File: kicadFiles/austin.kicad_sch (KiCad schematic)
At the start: 558 parts, among them J1 Conn_01x04, J2 ARM SWD, J3 TYPE-C-31-M12, Q1 DTC123J, Q2 AO3401A, Q3 DTC123JKAT146, SW1 SW_Push, SW10 MXSwitch, SW100 MXSwitch, SW101 MXSwitch, SW102 MXSwitch, SW103 MXSwitch, SW104 MXSwitch, SW105 MXSwitch, SW106 MXSwitch, SW107 MXSwitch, SW108 MXSwitch, SW109 MXSwitch, SW11 MXSwitch, SW110 MXSwitch, SW111 MXSwitch, SW112 MXSwitch, SW113 MXSwitch, SW114 MXSwitch, SW115 MXSwitch, SW116 MXSwitch, SW12 MXSwitch, SW13 MXSwitch, SW14 MXSwitch, SW15 MXSwitch, SW16 MXSwitch, SW17 MXSwitch, SW18 MXSwitch, SW19 MXSwitch, SW2 PCM12SMTR, SW20 MXSwitch, SW21 MXSwitch, SW22 MXSwitch, SW23 MXSwitch, SW24 MXSwitch, SW25 MXSwitch, SW26 MXSwitch, SW27 MXSwitch, SW28 MXSwitch, SW29 MXSwitch, SW3 MXSwitch, SW30 MXSwitch, SW31 MXSwitch, SW32 MXSwitch, SW33 MXSwitch, SW34 MXSwitch, SW35 MXSwitch, SW36 MXSwitch, SW37 MXSwitch, SW38 MXSwitch, SW39 MXSwitch, SW4 MXSwitch, SW40 MXSwitch, SW41 MXSwitch, SW42 MXSwitch, SW43 MXSwitch, SW44 MXSwitch, SW45 MXSwitch, SW46 MXSwitch, SW47 MXSwitch, SW48 MXSwitch, SW49 MXSwitch, SW5 MXSwitch, SW50 MXSwitch, SW51 MXSwitch, SW52 MXSwitch, SW53 MXSwitch, SW54 MXSwitch, SW55 MXSwitch, SW56 MXSwitch, SW57 MXSwitch, SW58 MXSwitch, SW59 MXSwitch, SW6 MXSwitch, SW60 MXSwitch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

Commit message: Remove switch symbols from bom
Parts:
- SW10, SW100, SW101, SW102, SW103, SW104, SW105, SW106, SW107, SW108, SW109, SW11, SW110, SW111, SW113, SW114, SW115, SW116, SW12, SW13, SW14, SW15, SW16, SW17, SW18, SW19, SW20, SW21, SW22, SW23, SW24, SW25, SW26, SW27, SW28, SW29, SW3, SW30, SW31, SW32, SW33, SW34, SW35, SW36, SW37, SW38, SW39, SW4, SW40, SW41, SW42, SW43, SW44, SW45, SW46, SW47, SW48, SW49, SW5, SW50, SW51, SW52, SW53, SW54, SW55, SW56, SW57, SW58, SW59, SW6, SW60, SW61, SW62, SW63, SW64, SW65, SW66, SW67, SW68, SW69, SW7, SW70, SW71, SW72, SW73, SW74, SW75, SW76, SW77, SW78, SW79, SW8, SW80, SW81, SW82, SW83, SW84, SW85, SW86, SW87, SW88, SW89, SW90, SW91, SW92, SW93, SW94, SW95, SW96, SW97, SW98, SW99: now left out of the parts list

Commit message: Add keyswitch metadata
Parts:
- LED4, LED5: now left out of the parts list
- SW10: symbol austin-rescue:MXSwitch-acheronSymbols-austin-rescue-austin-rescue -> acheronSymbols:MXSwitch; Keycode (none) -> F7; now in the parts list
- SW100: symbol austin-rescue:MXSwitch-acheronSymbols-austin-rescue-austin-rescue -> acheronSymbols:MXSwitch; Keycode (none) -> NPLUS; now in the parts list
- SW101: symbol austin-rescue:MXSwitch-acheronSymbols-austin-rescue-austin-rescue -> acheronSymbols:MXSwitch; Keycode (none) -> (625) LCTRL; now in the parts list
- SW102: symbol austin-rescue:MXSwitch-acheronSymbols-austin-rescue-austin-rescue -> acheronSymbols:MXSwitch; Keycode (none) -> (625) LWIN; now in the parts list
- SW103: symbol austin-rescue:MXSwitch-acheronSymbols-austin-rescue-austin-rescue -> acheronSymbols:MXSwitch; Keycode (none) -> (625) SPC; now in the parts list
- SW104: symbol austin-rescue:MXSwitch-acheronSymbols-austin-rescue-austin-rescue -> acheronSymbols:MXSwitch; Keycode (none) -> RALT; now in the parts list
- SW105: symbol austin-rescue:MXSwitch-acheronSymbols-austin-rescue-austin-rescue -> acheronSymbols:MXSwitch; Keycode (none) -> RWIN; now in the parts list
- SW106: symbol austin-rescue:MXSwitch-acheronSymbols-austin-rescue-austin-rescue -> acheronSymbols:MXSwitch; Keycode (none) -> LEFT; now in the parts list
- SW107: symbol austin-rescue:MXSwitch-acheronSymbols-austin-rescue-austin-rescue -> acheronSymbols:MXSwitch; Keycode (none) -> DOWN; now in the parts list
- SW108: symbol austin-rescue:MXSwitch-acheronSymbols-austin-rescue-austin-rescue -> acheronSymbols:MXSwitch; Keycode (none) -> LZERO; now in the parts list
- SW109: symbol austin-rescue:MXSwitch-acheronSymbols-austin-rescue-austin-rescue -> acheronSymbols:MXSwitch; Keycode (none) -> RZERO; now in the parts list
- SW11: symbol austin-rescue:MXSwitch-acheronSymbols-austin-rescue-austin-rescue -> acheronSymbols:MXSwitch; Keycode (none) -> F8; now in the parts list
- SW110: symbol austin-rescue:MXSwitch-acheronSymbols-austin-rescue-austin-rescue -> acheronSymbols:MXSwitch; Keycode (none) -> N0; now in the parts list
- SW111: symbol austin-rescue:MXSwitch-acheronSymbols-austin-rescue-austin-rescue -> acheronSymbols:MXSwitch; Keycode (none) -> (700) RCTRL; now in the parts list
- SW112: symbol austin-rescue:MXSwitch-acheronSymbols-austin-rescue-austin-rescue -> acheronSymbols:MXSwitch; Keycode (none) -> (700) LALT
- SW113: symbol austin-rescue:MXSwitch-acheronSymbols-austin-rescue-austin-rescue -> acheronSymbols:MXSwitch; Keycode (none) -> (625) LALT; now in the parts list
- SW114: symbol austin-rescue:MXSwitch-acheronSymbols-austin-rescue-austin-rescue -> acheronSymbols:MXSwitch; Keycode (none) -> (700) SPC; now in the parts list
- SW115: symbol austin-rescue:MXSwitch-acheronSymbols-austin-rescue-austin-rescue -> acheronSymbols:MXSwitch; Keycode (none) -> RIGHT; now in the parts list
- SW116: symbol austin-rescue:MXSwitch-acheronSymbols-austin-rescue-austin-rescue -> acheronSymbols:MXSwitch; Keycode (none) -> 2UZERO; now in the parts list
- SW12: symbol austin-rescue:MXSwitch-acheronSymbols-austin-rescue-austin-rescue -> acheronSymbols:MXSwitch; Keycode (none) -> F9; now in the parts list
- SW13: symbol austin-rescue:MXSwitch-acheronSymbols-austin-rescue-austin-rescue -> acheronSymbols:MXSwitch; Keycode (none) -> F10; now in the parts list
- SW14: symbol austin-rescue:MXSwitch-acheronSymbols-austin-rescue-austin-rescue -> acheronSymbols:MXSwitch; Keycode (none) -> F11; now in the parts list
- SW15: symbol austin-rescue:MXSwitch-acheronSymbols-austin-rescue-austin-rescue -> acheronSymbols:MXSwitch; Keycode (none) -> F12; now in the parts list
- SW16: symbol austin-rescue:MXSwitch-acheronSymbols-austin-rescue-austin-rescue -> acheronSymbols:MXSwitch; Keycode (none) -> F13; now in the parts list
- SW17: symbol austin-rescue:MXSwitch-acheronSymbols-austin-rescue-austin-rescue -> acheronSymbols:MXSwitch; Keycode (none) -> SCRLK; now in the parts list
- SW18: symbol austin-rescue:MXSwitch-acheronSymbols-austin-rescue-austin-rescue -> acheronSymbols:MXSwitch; Keycode (none) -> PAUSE; now in the parts list
- SW19: symbol austin-rescue:MXSwitch-acheronSymbols-austin-rescue-austin-rescue -> acheronSymbols:MXSwitch; Keycode (none) -> HOME; now in the parts list
- SW20: symbol austin-rescue:MXSwitch-acheronSymbols-austin-rescue-austin-rescue -> acheronSymbols:MXSwitch; Keycode (none) -> END; now in the parts list
- SW21: symbol austin-rescue:MXSwitch-acheronSymbols-austin-rescue-austin-rescue -> acheronSymbols:MXSwitch; Keycode (none) -> DELETE; now in the parts list
- SW22: symbol austin-rescue:MXSwitch-acheronSymbols-austin-rescue-austin-rescue -> acheronSymbols:MXSwitch; Keycode (none) -> GRAVE; now in the parts list
- SW23: symbol austin-rescue:MXSwitch-acheronSymbols-austin-rescue-austin-rescue -> acheronSymbols:MXSwitch; Keycode (none) -> 1; now in the parts list
- SW24: symbol austin-rescue:MXSwitch-acheronSymbols-austin-rescue-austin-rescue -> acheronSymbols:MXSwitch; Keycode (none) -> 2; now in the parts list
- SW25: symbol austin-rescue:MXSwitch-acheronSymbols-austin-rescue-austin-rescue -> acheronSymbols:MXSwitch; Keycode (none) -> 3; now in the parts list
- SW26: symbol austin-rescue:MXSwitch-acheronSymbols-austin-rescue-austin-rescue -> acheronSymbols:MXSwitch; Keycode (none) -> 4; now in the parts list
- SW27: symbol austin-rescue:MXSwitch-acheronSymbols-austin-rescue-austin-rescue -> acheronSymbols:MXSwitch; Keycode (none) -> 5; now in the parts list
- SW28: symbol austin-rescue:MXSwitch-acheronSymbols-austin-rescue-austin-rescue -> acheronSymbols:MXSwitch; Keycode (none) -> 6; now in the parts list
- SW29: symbol austin-rescue:MXSwitch-acheronSymbols-austin-rescue-austin-rescue -> acheronSymbols:MXSwitch; Keycode (none) -> 7; now in the parts list
- SW3: symbol austin-rescue:MXSwitch-acheronSymbols-austin-rescue-austin-rescue -> acheronSymbols:MXSwitch; Keycode (none) -> ESC; now in the parts list
- SW30: symbol austin-rescue:MXSwitch-acheronSymbols-austin-rescue-austin-rescue -> acheronSymbols:MXSwitch; Keycode (none) -> 8; now in the parts list
- SW31: symbol austin-rescue:MXSwitch-acheronSymbols-austin-rescue-austin-rescue -> acheronSymbols:MXSwitch; Keycode (none) -> 9; now in the parts list
- SW32: symbol austin-rescue:MXSwitch-acheronSymbols-austin-rescue-austin-rescue -> acheronSymbols:MXSwitch; Keycode (none) -> 0; now in the parts list
- SW33: symbol austin-rescue:MXSwitch-acheronSymbols-austin-rescue-austin-rescue -> acheronSymbols:MXSwitch; Keycode (none) -> MINUS; now in the parts list
- SW34: symbol austin-rescue:MXSwitch-acheronSymbols-austin-rescue-austin-rescue -> acheronSymbols:MXSwitch; Keycode (none) -> EQL; now in the parts list
- SW35: symbol austin-rescue:MXSwitch-acheronSymbols-austin-rescue-austin-rescue -> acheronSymbols:MXSwitch; Keycode (none) -> LBKSP; now in the parts list
- SW36: symbol austin-rescue:MXSwitch-acheronSymbols-austin-rescue-austin-rescue -> acheronSymbols:MXSwitch; Keycode (none) -> RBKSP; now in the parts list
- SW37: symbol austin-rescue:MXSwitch-acheronSymbols-austin-rescue-austin-rescue -> acheronSymbols:MXSwitch; Keycode (none) -> INS; now in the parts list
- SW38: symbol austin-rescue:MXSwitch-acheronSymbols-austin-rescue-austin-rescue -> acheronSymbols:MXSwitch; Keycode (none) -> NUMLK; now in the parts list
- SW39: symbol austin-rescue:MXSwitch-acheronSymbols-austin-rescue-austin-rescue -> acheronSymbols:MXSwitch; Keycode (none) -> NSLS; now in the parts list
- SW4: symbol austin-rescue:MXSwitch-acheronSymbols-austin-rescue-austin-rescue -> acheronSymbols:MXSwitch; Keycode (none) -> F1; now in the parts list
- SW40: symbol austin-rescue:MXSwitch-acheronSymbols-austin-rescue-austin-rescue -> acheronSymbols:MXSwitch; Keycode (none) -> NMUL; now in the parts list
- SW41: symbol austin-rescue:MXSwitch-acheronSymbols-austin-rescue-austin-rescue -> acheronSymbols:MXSwitch; Keycode (none) -> FULLBKSP; now in the parts list
- SW42: symbol austin-rescue:MXSwitch-acheronSymbols-austin-rescue-austin-rescue -> acheronSymbols:MXSwitch; Keycode (none) -> ISOENTER; now in the parts list
- SW43: symbol austin-rescue:MXSwitch-acheronSymbols-austin-rescue-austin-rescue -> acheronSymbols:MXSwitch; Keycode (none) -> TAB; now in the parts list
- SW44: symbol austin-rescue:MXSwitch-acheronSymbols-austin-rescue-austin-rescue -> acheronSymbols:MXSwitch; Keycode (none) -> Q; now in the parts list
- SW45: symbol austin-rescue:MXSwitch-acheronSymbols-austin-rescue-austin-rescue -> acheronSymbols:MXSwitch; Keycode (none) -> W; now in the parts list
- SW46: symbol austin-rescue:MXSwitch-acheronSymbols-austin-rescue-austin-rescue -> acheronSymbols:MXSwitch; Keycode (none) -> E; now in the parts list
- SW47: symbol austin-rescue:MXSwitch-acheronSymbols-austin-rescue-austin-rescue -> acheronSymbols:MXSwitch; Keycode (none) -> R; now in the parts list
- SW48: symbol austin-rescue:MXSwitch-acheronSymbols-austin-rescue-austin-rescue -> acheronSymbols:MXSwitch; Keycode (none) -> T; now in the parts list
- SW49: symbol austin-rescue:MXSwitch-acheronSymbols-austin-rescue-austin-rescue -> acheronSymbols:MXSwitch; Keycode (none) -> Y; now in the parts list
- SW5: symbol austin-rescue:MXSwitch-acheronSymbols-austin-rescue-austin-rescue -> acheronSymbols:MXSwitch; Keycode (none) -> F2; now in the parts list
- SW50: symbol austin-rescue:MXSwitch-acheronSymbols-austin-rescue-austin-rescue -> acheronSymbols:MXSwitch; Keycode (none) -> U; now in the parts list
- SW51: symbol austin-rescue:MXSwitch-acheronSymbols-austin-rescue-austin-rescue -> acheronSymbols:MXSwitch; Keycode (none) -> I; now in the parts list
- SW52: symbol austin-rescue:MXSwitch-acheronSymbols-austin-rescue-austin-rescue -> acheronSymbols:MXSwitch; Keycode (none) -> O; now in the parts list
- SW53: symbol austin-rescue:MXSwitch-acheronSymbols-austin-rescue-austin-rescue -> acheronSymbols:MXSwitch; Keycode (none) -> P; now in the parts list
- SW54: symbol austin-rescue:MXSwitch-acheronSymbols-austin-rescue-austin-rescue -> acheronSymbols:MXSwitch; Keycode (none) -> LBRKT; now in the parts list
- SW55: symbol austin-rescue:MXSwitch-acheronSymbols-austin-rescue-austin-rescue -> acheronSymbols:MXSwitch; Keycode (none) -> RBRKT; now in the parts list
- SW56: symbol austin-rescue:MXSwitch-acheronSymbols-austin-rescue-austin-rescue -> acheronSymbols:MXSwitch; Keycode (none) -> BSLS; now in the parts list
- SW57: symbol austin-rescue:MXSwitch-acheronSymbols-austin-rescue-austin-rescue -> acheronSymbols:MXSwitch; Keycode (none) -> PGUP; now in the parts list
- SW58: symbol austin-rescue:MXSwitch-acheronSymbols-austin-rescue-austin-rescue -> acheronSymbols:MXSwitch; Keycode (none) -> N7; now in the parts list
- SW59: symbol austin-rescue:MXSwitch-acheronSymbols-austin-rescue-austin-rescue -> acheronSymbols:MXSwitch; Keycode (none) -> N8; now in the parts list
- SW6: symbol austin-rescue:MXSwitch-acheronSymbols-austin-rescue-austin-rescue -> acheronSymbols:MXSwitch; Keycode (none) -> F3; now in the parts list
- SW60: symbol austin-rescue:MXSwitch-acheronSymbols-austin-rescue-austin-rescue -> acheronSymbols:MXSwitch; Keycode (none) -> N9; now in the parts list
- SW61: symbol austin-rescue:MXSwitch-acheronSymbols-austin-rescue-austin-rescue -> acheronSymbols:MXSwitch; Keycode (none) -> NMINUS; now in the parts list
- SW62: symbol austin-rescue:MXSwitch-acheronSymbols-austin-rescue-austin-rescue -> acheronSymbols:MXSwitch; Keycode (none) -> ISOTILDE; now in the parts list
- SW63: symbol austin-rescue:MXSwitch-acheronSymbols-austin-rescue-austin-rescue -> acheronSymbols:MXSwitch; Keycode (none) -> CAPS; now in the parts list
- SW64: symbol austin-rescue:MXSwitch-acheronSymbols-austin-rescue-austin-rescue -> acheronSymbols:MXSwitch; Keycode (none) -> A; now in the parts list
- SW65: symbol austin-rescue:MXSwitch-acheronSymbols-austin-rescue-austin-rescue -> acheronSymbols:MXSwitch; Keycode (none) -> S; now in the parts list
- SW66: symbol austin-rescue:MXSwitch-acheronSymbols-austin-rescue-austin-rescue -> acheronSymbols:MXSwitch; Keycode (none) -> D; now in the parts list
- SW67: symbol austin-rescue:MXSwitch-acheronSymbols-austin-rescue-austin-rescue -> acheronSymbols:MXSwitch; Keycode (none) -> F; now in the parts list
- SW68: symbol austin-rescue:MXSwitch-acheronSymbols-austin-rescue-austin-rescue -> acheronSymbols:MXSwitch; Keycode (none) -> G; now in the parts list
- SW69: symbol austin-rescue:MXSwitch-acheronSymbols-austin-rescue-austin-rescue -> acheronSymbols:MXSwitch; Keycode (none) -> H; now in the parts list
- SW7: symbol austin-rescue:MXSwitch-acheronSymbols-austin-rescue-austin-rescue -> acheronSymbols:MXSwitch; Keycode (none) -> F4; now in the parts list
- SW70: symbol austin-rescue:MXSwitch-acheronSymbols-austin-rescue-austin-rescue -> acheronSymbols:MXSwitch; Keycode (none) -> J; now in the parts list
- SW71: symbol austin-rescue:MXSwitch-acheronSymbols-austin-rescue-austin-rescue -> acheronSymbols:MXSwitch; Keycode (none) -> K; now in the parts list
- SW72: symbol austin-rescue:MXSwitch-acheronSymbols-austin-rescue-austin-rescue -> acheronSymbols:MXSwitch; Keycode (none) -> L; now in the parts list
- SW73: symbol austin-rescue:MXSwitch-acheronSymbols-austin-rescue-austin-rescue -> acheronSymbols:MXSwitch; Keycode (none) -> COLON; now in the parts list
- SW74: symbol austin-rescue:MXSwitch-acheronSymbols-austin-rescue-austin-rescue -> acheronSymbols:MXSwitch; Keycode (none) -> QUOTE; now in the parts list
- SW75: symbol austin-rescue:MXSwitch-acheronSymbols-austin-rescue-austin-rescue -> acheronSymbols:MXSwitch; Keycode (none) -> ANSIENTER; now in the parts list
- SW76: symbol austin-rescue:MXSwitch-acheronSymbols-austin-rescue-austin-rescue -> acheronSymbols:MXSwitch; Keycode (none) -> PGDN; now in the parts list
- SW77: symbol austin-rescue:MXSwitch-acheronSymbols-austin-rescue-austin-rescue -> acheronSymbols:MXSwitch; Keycode (none) -> N4; now in the parts list
- SW78: symbol austin-rescue:MXSwitch-acheronSymbols-austin-rescue-austin-rescue -> acheronSymbols:MXSwitch; Keycode (none) -> N5; now in the parts list
- SW79: symbol austin-rescue:MXSwitch-acheronSymbols-austin-rescue-austin-rescue -> acheronSymbols:MXSwitch; Keycode (none) -> N6; now in the parts list
- SW8: symbol austin-rescue:MXSwitch-acheronSymbols-austin-rescue-austin-rescue -> acheronSymbols:MXSwitch; Keycode (none) -> F5; now in the parts list
- SW80: symbol austin-rescue:MXSwitch-acheronSymbols-austin-rescue-austin-rescue -> acheronSymbols:MXSwitch; Keycode (none) -> NENTER; now in the parts list
- SW81: symbol austin-rescue:MXSwitch-acheronSymbols-austin-rescue-austin-rescue -> acheronSymbols:MXSwitch; Keycode (none) -> STEPPEDCAPS; now in the parts list
- SW82: value ANSI LShift -> MXSwitch; symbol austin-rescue:MXSwitch-acheronSymbols-austin-rescue-austin-rescue -> acheronSymbols:MXSwitch; Keycode (none) -> ANSISHIFT; now in the parts list
- SW83: symbol austin-rescue:MXSwitch-acheronSymbols-austin-rescue-austin-rescue -> acheronSymbols:MXSwitch; Keycode (none) -> RSFT; now in the parts list
- SW84: value ISO LShift -> MXSwitch; symbol austin-rescue:MXSwitch-acheronSymbols-austin-rescue-austin-rescue -> acheronSymbols:MXSwitch; Keycode (none) -> ISOSHIFT; now in the parts list
- SW85: value ISO Slash -> MXSwitch; symbol austin-rescue:MXSwitch-acheronSymbols-austin-rescue-austin-rescue -> acheronSymbols:MXSwitch; Keycode (none) -> ISOSLS; now in the parts list
- SW86: symbol austin-rescue:MXSwitch-acheronSymbols-austin-rescue-austin-rescue -> acheronSymbols:MXSwitch; Keycode (none) -> Z; now in the parts list
- SW87: symbol austin-rescue:MXSwitch-acheronSymbols-austin-rescue-austin-rescue -> acheronSymbols:MXSwitch; Keycode (none) -> X; now in the parts list
- SW88: symbol austin-rescue:MXSwitch-acheronSymbols-austin-rescue-austin-rescue -> acheronSymbols:MXSwitch; Keycode (none) -> C; now in the parts list
- SW89: symbol austin-rescue:MXSwitch-acheronSymbols-austin-rescue-austin-rescue -> acheronSymbols:MXSwitch; Keycode (none) -> V; now in the parts list
- SW9: symbol austin-rescue:MXSwitch-acheronSymbols-austin-rescue-austin-rescue -> acheronSymbols:MXSwitch; Keycode (none) -> F6
- SW90: symbol austin-rescue:MXSwitch-acheronSymbols-austin-rescue-austin-rescue -> acheronSymbols:MXSwitch; Keycode (none) -> B; now in the parts list
- SW91: symbol austin-rescue:MXSwitch-acheronSymbols-austin-rescue-austin-rescue -> acheronSymbols:MXSwitch; Keycode (none) -> N; now in the parts list
- SW92: symbol austin-rescue:MXSwitch-acheronSymbols-austin-rescue-austin-rescue -> acheronSymbols:MXSwitch; Keycode (none) -> M; now in the parts list
- SW93: symbol austin-rescue:MXSwitch-acheronSymbols-austin-rescue-austin-rescue -> acheronSymbols:MXSwitch; Keycode (none) -> COMMA; now in the parts list
- SW94: symbol austin-rescue:MXSwitch-acheronSymbols-austin-rescue-austin-rescue -> acheronSymbols:MXSwitch; Keycode (none) -> DOT; now in the parts list
- SW95: symbol austin-rescue:MXSwitch-acheronSymbols-austin-rescue-austin-rescue -> acheronSymbols:MXSwitch; Keycode (none) -> SLS; now in the parts list
- SW96: symbol austin-rescue:MXSwitch-acheronSymbols-austin-rescue-austin-rescue -> acheronSymbols:MXSwitch; Keycode (none) -> UP; now in the parts list
- SW97: symbol austin-rescue:MXSwitch-acheronSymbols-austin-rescue-austin-rescue -> acheronSymbols:MXSwitch; Keycode (none) -> N1; now in the parts list
- SW98: symbol austin-rescue:MXSwitch-acheronSymbols-austin-rescue-austin-rescue -> acheronSymbols:MXSwitch; Keycode (none) -> N2; now in the parts list
- SW99: symbol austin-rescue:MXSwitch-acheronSymbols-austin-rescue-austin-rescue -> acheronSymbols:MXSwitch; Keycode (none) -> N3; now in the parts list
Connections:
- net Col13: now also SW106.1 (Col)
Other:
- note removed: """
- note removed: "*"
- note removed: "+"
- note removed: "+="
- note removed: "-"
- note removed: "-_"
- note removed: "/"
- note removed: "0"
- note removed: "2"
- note removed: "3"
- note removed: "4"
- note removed: "5"
- note removed: "6"
- note removed: "7"
- note removed: "8"
- note removed: "9"
- note removed: ":;"
- note removed: "A"
- note removed: "B1LAlt"
- note removed: "B1RAlt"
- note removed: "B1RCtrl"
- note removed: "B1Spc"
- note removed: "B2LCtrl"
- note removed: "B2LWin"
- note removed: "B2Spc"
- note removed: "Backspace"
- note removed: "Caps"
- note removed: "D"
- note removed: "Del"
- note removed: "Delete"
- note removed: "Down"
- note removed: "End"
- note removed: "Enter"
- note removed: "Esc"
- note removed: "F1"
- note removed: "F10"
- note removed: "F11"
- note removed: "F12"
- note removed: "F2"
- note removed: "F3"
- note removed: "F4"
- note removed: "F5"
- note removed: "F6"
- note removed: "F7"
- note removed: "F8"
- note removed: "F9"
- note removed: "G"
- note removed: "GRAVE"
- note removed: "H"
- note removed: "Home"
- note removed: "ISO Enter"
- note removed: "ISO Tilde"
- note removed: "Insert"
- note removed: "J"
- note removed: "K"
- note removed: "L"
- note removed: "Left"
- note removed: "Numlock"
- note removed: "Pause"
- note removed: "PgDwn"
- note removed: "PgUp"
- note removed: "PrtSc"
- note removed: "R1Alt"
- note removed: "R1Win"
- note removed: "Right"
- note removed: "S"
- note removed: "ScrLck"
- note removed: "Split0L"
- note removed: "Split0R"
- note removed: "SplitBsL"
- note removed: "SplitBsR"
- note removed: "Stepped Caps"
- note removed: "\|"

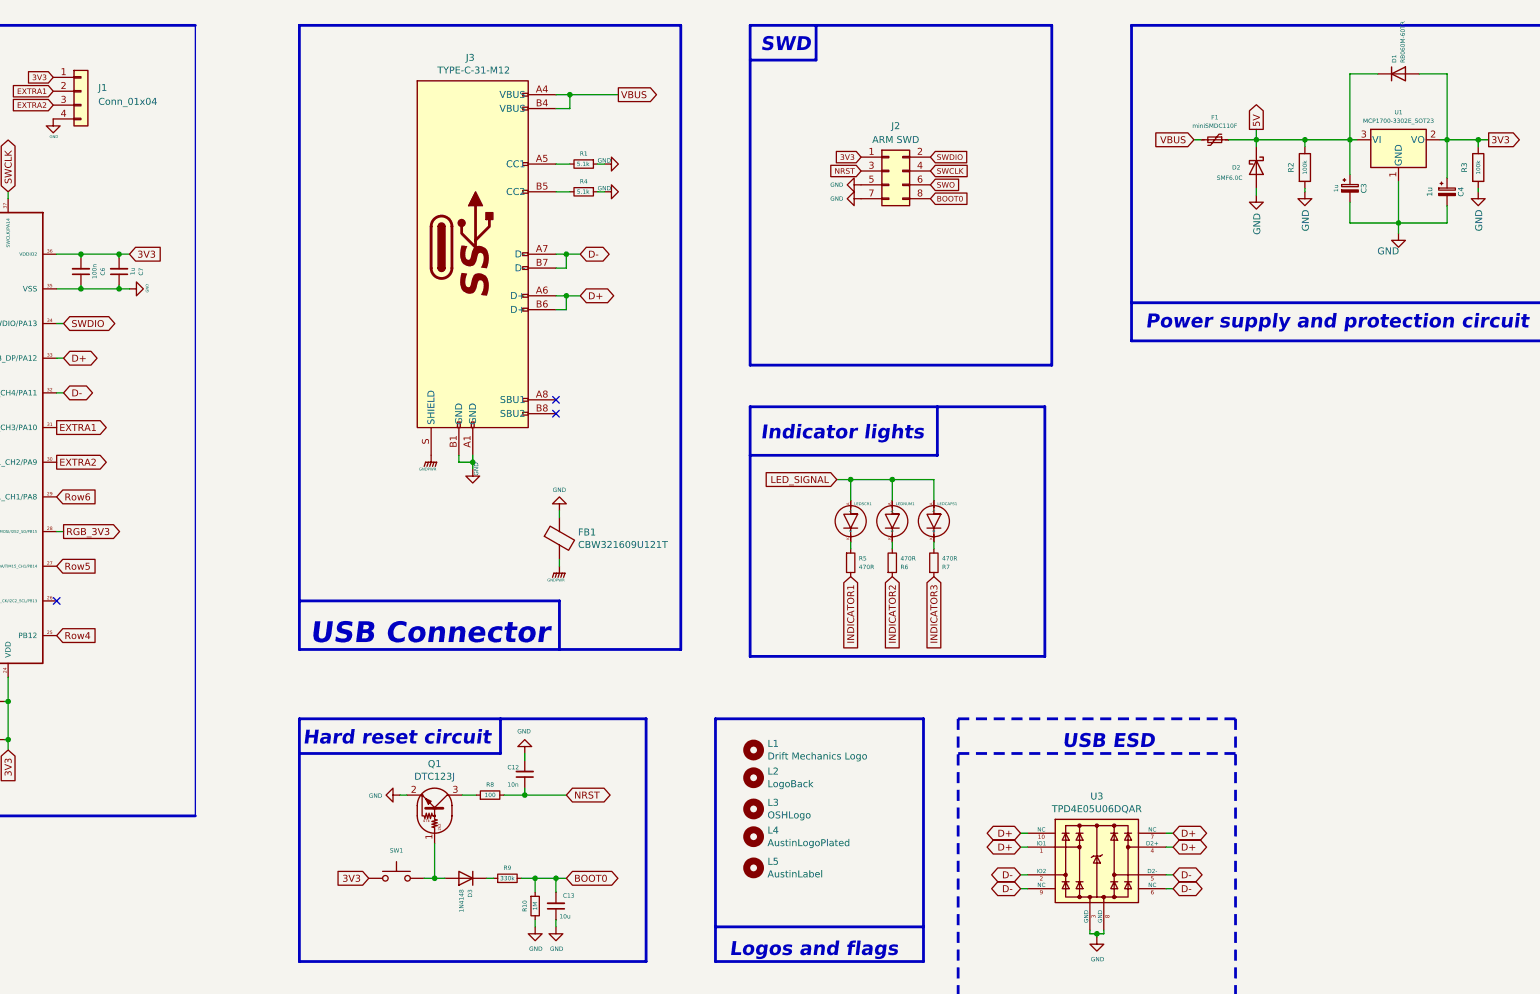
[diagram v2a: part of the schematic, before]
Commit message: Add component metadata, remove THT LEDs from BOM
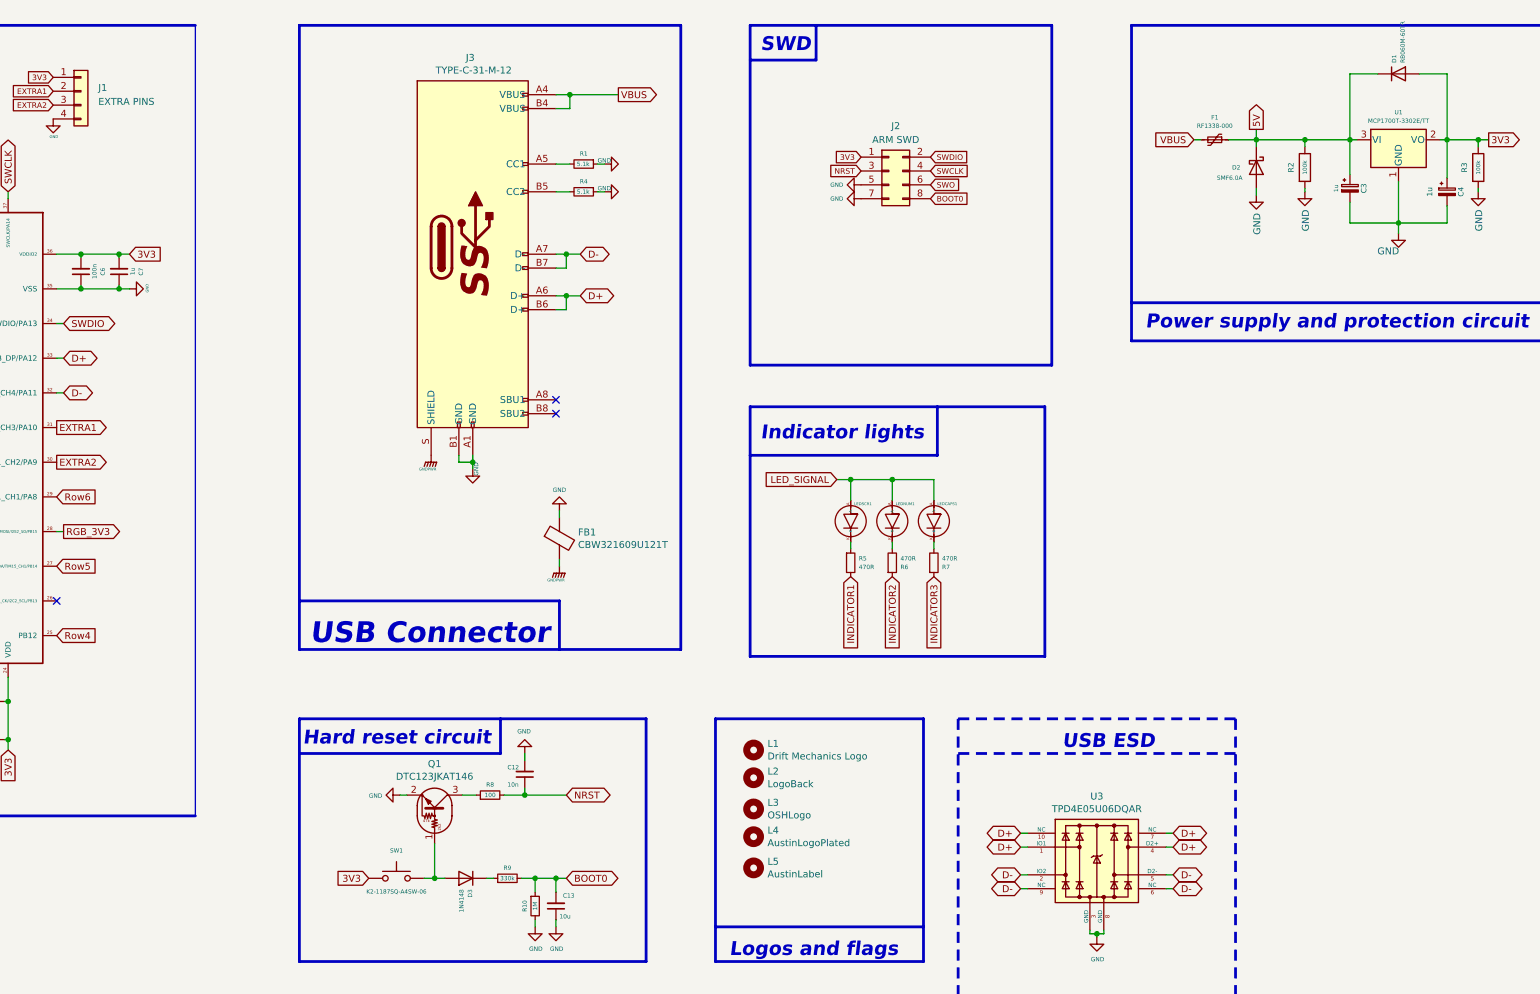
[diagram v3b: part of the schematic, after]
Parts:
- D1: LCSC Part Number (none) -> C114257; Manufacturer (none) -> ROHM; Manufacturer Part Number (none) -> RB060M-60TR; Package (none) -> SOD-123
- D2: value SMF6.0C -> SMF6.0A; LCSC Part Number (none) -> C362319; Manufacturer (none) -> LGE; Manufacturer Part Number (none) -> SMF6.0A; Package (none) -> SOD-123FL
- F1: value miniSMDC110F -> RF1338-000; Manufacturer Part Number miniSMDC110F -> RF1338-000
- J1: value Conn_01x04 -> EXTRA PINS; now left out of the parts list
- J2, LED10, LED100, LED101, LED102, LED103, LED104, LED105, LED106, LED107, LED108, LED109, LED11, LED110, LED111, LED112, LED113, LED114, LED115, LED12, LED13, LED14, LED15, LED16, LED17, LED18, LED19, LED20, LED21, LED22, LED23, LED24, LED25, LED26, LED27, LED28, LED29, LED3, LED30, LED31, LED32, LED33, LED34, LED35, LED36, LED37, LED38, LED39, LED40, LED41, LED42, LED43, LED44, LED45, LED46, LED47, LED48, LED49, LED50, LED51, LED52, LED53, LED54, LED55, LED56, LED57, LED58, LED59, LED6, LED60, LED61, LED62, LED63, LED64, LED65, LED66, LED68, LED69, LED7, LED70, LED71, LED72, LED73, LED74, LED75, LED76, LED77, LED78, LED79, LED8, LED80, LED81, LED82, LED83, LED84, LED85, LED86, LED87, LED88, LED89, LED9, LED90, LED91, LED92, LED93, LED94, LED95, LED96, LED97, LED98, LED99, LEDCAPS1, LEDNUM1, LEDSCR1: now left out of the parts list
- J3: value TYPE-C-31-M12 -> TYPE-C-31-M-12; LCSC Part Number (none) -> C2760486; Manufacturer (none) -> Korean Hroparts; Manufacturer Part Number (none) -> TYPE-C-31-M-12
- Q1: value DTC123J -> DTC123JKAT146; LCSC Part Number (none) -> C111724; Manufacturer (none) -> ROHM; Manufacturer Part Number (none) -> DTC123JKAT146; Package (none) -> SOT-23
- SW1: value SW_Push -> K2-1187SQ-A4SW-06; LCSC Part Number (none) -> C92584; Manufacturer (none) -> Korean Hroparts; Manufacturer Part Number (none) -> K2-1187SQ-A4SW-06
- U1: value MCP1700-3302E_SOT23 -> MCP1700T-3302E/TT

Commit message: Add further component metadata
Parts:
- C14, C15, C16, C17, C18, C19, C20, C21, C22, C23, C24, C25, C26, C27, C28, C29, C30, C31, C32, C33, C34, C35: Rating MLCC 0805 10V or more -> (none)
- C3, C4: Package (none) -> C3216 CASEA
- D100, D101, D102, D103, D104, D105, D106, D107, D108, D109, D110, D111, D112, D113, D114, D115, D116, D117, D118, D119, D120, D121, D122, D123, D124, D125, D126, D127, D128, D24, D25, D26, D27, D28, D29, D3, D30, D31, D32, D33, D34, D35, D36, D37, D38, D39, D40, D41, D42, D43, D44, D45, D46, D47, D48, D49, D50, D51, D52, D53, D54, D55, D56, D57, D58, D59, D60, D61, D62, D63, D64, D65, D66, D67, D68, D69, D70, D71, D72, D73, D74, D75, D76, D77, D78, D79, D80, D81, D82, D83, D84, D85, D86, D87, D88, D89, D90, D91, D92, D93, D94, D95, D96, D97, D98, D99: value 1N4148 -> 1N4148W; Package (none) -> SOD-123
- SW2: Specification Surface mount SPDT switch -> (none)
